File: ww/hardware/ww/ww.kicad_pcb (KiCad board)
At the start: 2 copper layers, 31 x 38 mm, 49 parts, among them J1 USB_B, J2 Conn_ARM_JTAG_SWD_10, SW1 BTN0, SW2 BTN1, U1 MCP73812T-420I-OT, U10 APA102, U11 APA102, U12 APA102, U13 APA102, U14 APA102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

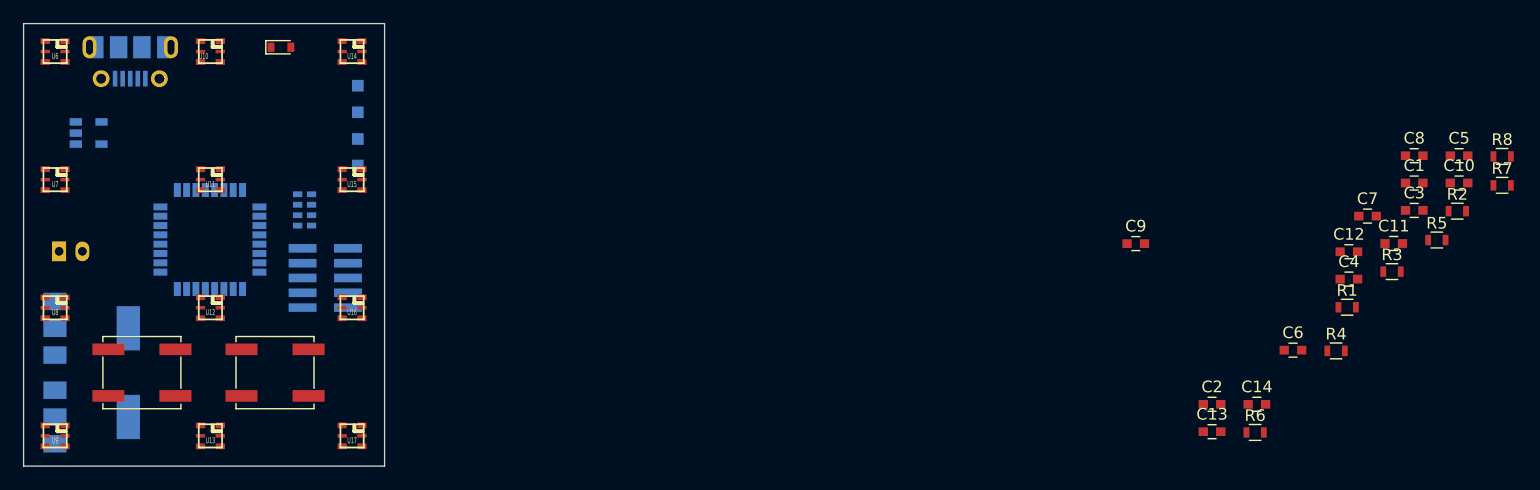
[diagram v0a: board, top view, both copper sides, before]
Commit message: Place remaining passives, no tracks yet
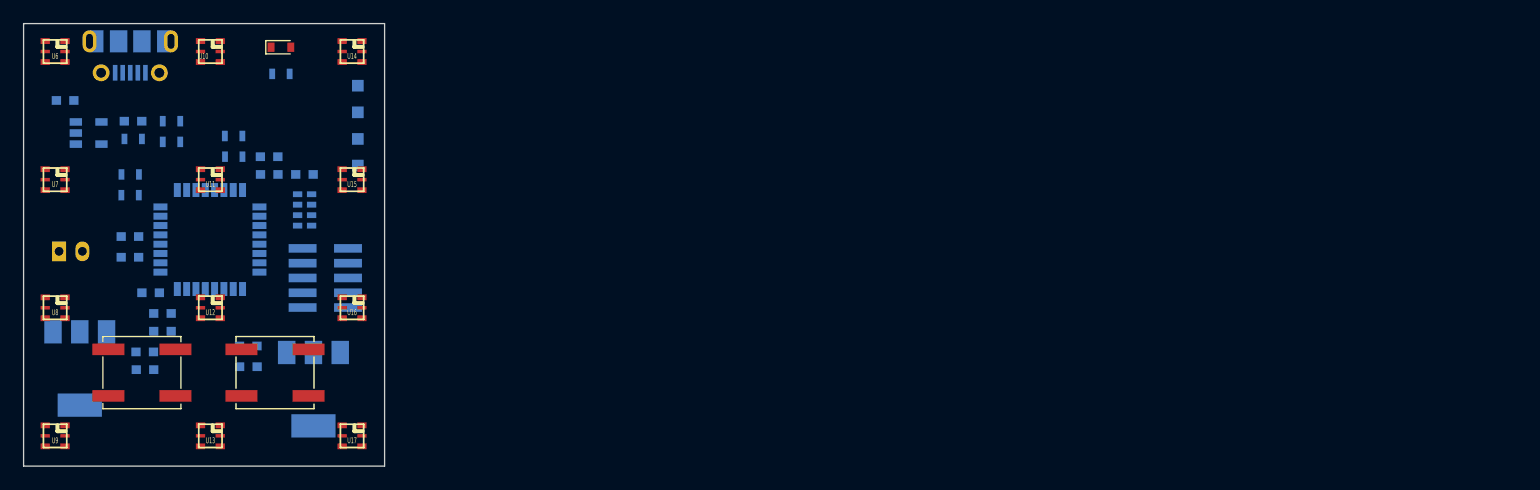
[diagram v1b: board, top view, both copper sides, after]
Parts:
- C1, C10, C11, C12, C13, C14, C2, C3, C4, C5, C6, C7, C8, C9, R1, R2, R3, R4, R5, R6, R7, R8: moved to B.Cu
- moved C3 116.2 mm to (41.7, 31.2)
- moved C5 113.0 mm to (49.0, 47.8), turned to 180 degrees
- moved R5 112.3 mm to (47.2, 39.4), turned to 180 degrees
- moved C10 112.1 mm to (50.0, 51.1), turned to 180 degrees
- moved R2 110.7 mm to (50.8, 33.0)
- moved R8 108.9 mm to (56.1, 34.3), turned to 180 degrees
- moved C7 105.6 mm to (48.5, 52.8)
- moved R3 105.4 mm to (50.8, 34.8), turned to 180 degrees
- moved R7 105.3 mm to (60.2, 29.0)
- moved R1 105.2 mm to (47.5, 34.5)
- moved R4 104.7 mm to (47.3, 37.6)
- moved C12 103.9 mm to (48.5, 54.4)
- moved C11 98.9 mm to (57.4, 54.1), turned to 180 degrees
- moved C8 98.3 mm to (59.2, 36.1)
- moved C14 97.6 mm to (47.2, 44.7), turned to 180 degrees
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
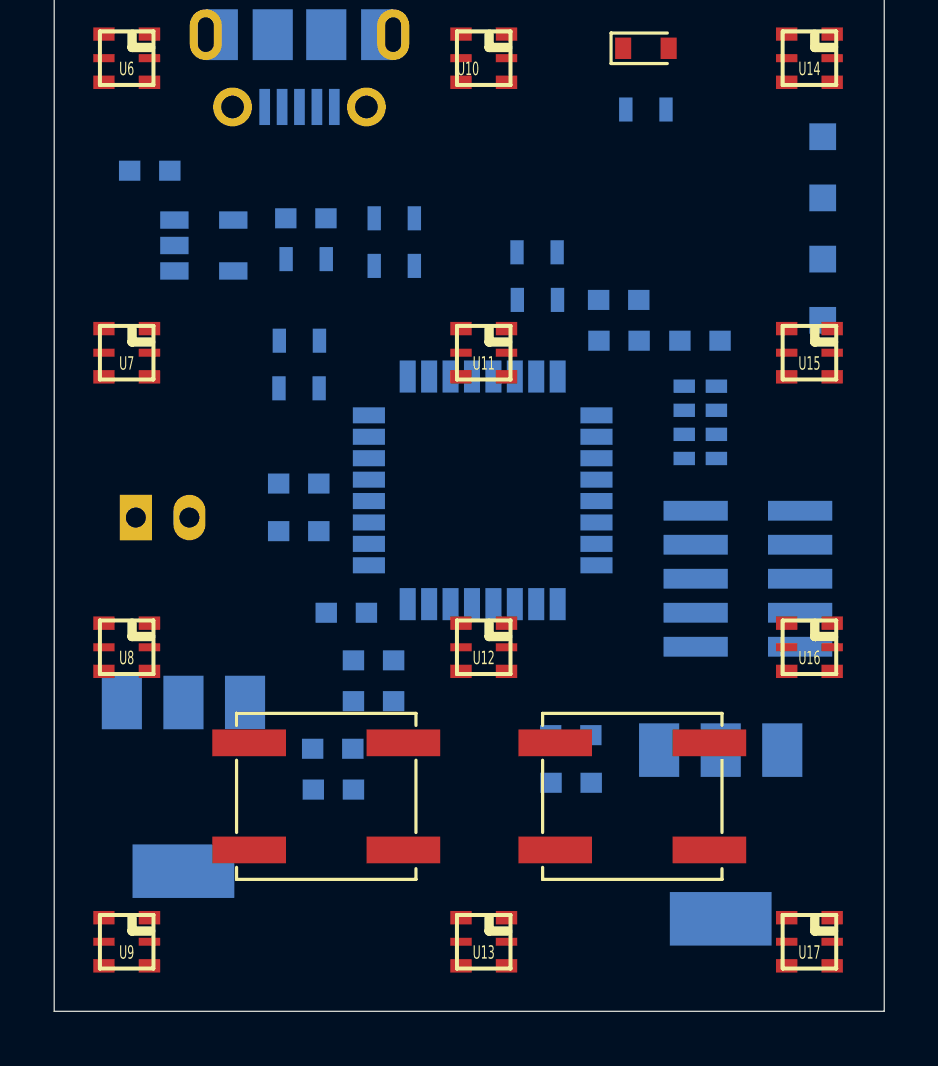
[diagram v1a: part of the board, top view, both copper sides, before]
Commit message: Use side-angled SMT JST battery connector
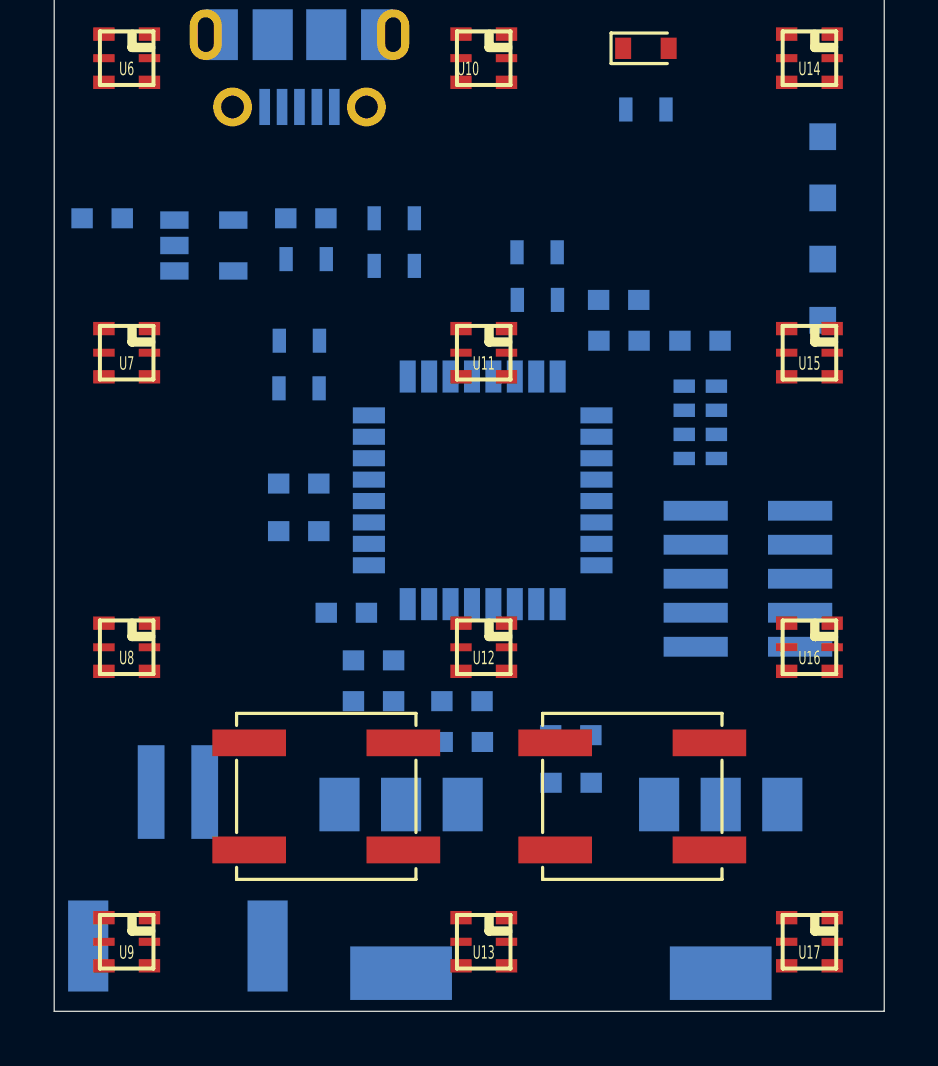
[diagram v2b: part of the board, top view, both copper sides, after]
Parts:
- BT1: footprint Connectors_JST:JST_PH_B2B-PH-K_02x2.00mm_Straight -> Connectors_JST:JST_PH_S2B-PH-SM4-TB_02x2.00mm_Angled
- moved BT1 13.2 mm to (42.7, 57.3), turned to 180 degrees
- moved U4 8.98 mm to (51.1, 58.1)
- moved C7 5.14 mm to (53.3, 51.1)
- moved C12 5.13 mm to (53.3, 52.6)
- moved C3 2.51 mm to (39.9, 33.0)
- moved U3 2.03 mm to (63.0, 58.1)
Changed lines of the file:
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@@
     (add_net "Net-(U5-Pad9)")
-  )
-  (module Connectors_JST:JST_PH_B2B-PH-K_02x2.00mm_Straight (layer B.Cu)
-    (at 41.148 44.196)
-    (descr "JST PH series connector, B2B-PH-K, top entry type, through hole, Datasheet: http://www.jst-mfg.com/product/pdf/eng/ePH.pdf")
-    (tags "connector jst ph")
-    (fp_text reference BT1 (at 1.5 2.8) (layer B.SilkS)
-      (effects (font (size 1 1) (thickness 0.15)) (justify mirror))
-    )
-    (fp_text value Battery_Cell (at 1 -3.8) (layer B.Fab)
-      (effects (font (size 1 1) (thickness 0.15)) (justify mirror))
-    )
-    (fp_text user %R (at 1 -1.5) (layer B.Fab)
-      (effects (font (size 1 1) (thickness 0.15)) (justify mirror))
-    )
-    (fp_line (start 4.45 2.2) (end -2.45 2.2) (layer B.CrtYd) (width 0.05))
-    (fp_line (start 4.45 -3.3) (end 4.45 2.2) (layer B.CrtYd) (width 0.05))
-    (fp_line (start -2.45 -3.3) (end 4.45 -3.3) (layer B.CrtYd) (width 0.05))
-    (fp_line (start -2.45 2.2) (end -2.45 -3.3) (layer B.CrtYd) (width 0.05))
-    (fp_line (start 3.95 1.7) (end -1.95 1.7) (layer B.Fab) (width 0.1))
-    (fp_line (start 3.95 -2.8) (end 3.95 1.7) (layer B.Fab) (width 0.1))
-    (fp_line (start -1.95 -2.8) (end 3.95 -2.8) (layer B.Fab) (width 0.1))
-    (fp_line (start -1.95 1.7) (end -1.95 -2.8) (layer B.Fab) (width 0.1))
-    (fp_line (start -2.35 2.1) (end -2.35 0.85) (layer B.Fab) (width 0.1))
-    (fp_line (start -1.1 2.1) (end -2.35 2.1) (layer B.Fab) (width 0.1))
-    (fp_line (start -2.35 2.1) (end -2.35 0.85) (layer B.SilkS) (width 0.12))
-    (fp_line (start -1.1 2.1) (end -2.35 2.1) (layer B.SilkS) (width 0.12))
-    (fp_line (start 1 -2.3) (end 1 -1.8) (layer B.SilkS) (width 0.12))
-    (fp_line (start 1.1 -1.8) (end 1.1 -2.3) (layer B.SilkS) (width 0.12))
-    (fp_line (start 0.9 -1.8) (end 1.1 -1.8) (layer B.SilkS) (width 0.12))
-    (fp_line (start 0.9 -2.3) (end 0.9 -1.8) (layer B.SilkS) (width 0.12))
-    (fp_line (start -0.3 1.9) (end -0.6 1.9) (layer B.SilkS) (width 0.12))
-    (fp_line (start -0.6 2) (end -0.6 1.8) (layer B.SilkS) (width 0.12))
-    (fp_line (start -0.3 2) (end -0.6 2) (layer B.SilkS) (width 0.12))
-    (fp_line (start -0.3 1.8) (end -0.3 2) (layer B.SilkS) (width 0.12))
-    (fp_line (start 4.05 -0.8) (end 3.45 -0.8) (layer B.SilkS) (width 0.12))
-    (fp_line (start 4.05 0.5) (end 3.45 0.5) (layer B.SilkS) (width 0.12))
-    (fp_line (start -2.05 -0.8) (end -1.45 -0.8) (layer B.SilkS) (width 0.12))
-    (fp_line (start -2.05 0.5) (end -1.45 0.5) (layer B.SilkS) (width 0.12))
-    (fp_line (start 1.5 1.2) (end 1.5 1.8) (layer B.SilkS) (width 0.12))
-    (fp_line (start 3.45 1.2) (end 1.5 1.2) (layer B.SilkS) (width 0.12))
-    (fp_line (start 3.45 -2.3) (end 3.45 1.2) (layer B.SilkS) (width 0.12))
-    (fp_line (start -1.45 -2.3) (end 3.45 -2.3) (layer B.SilkS) (width 0.12))
-    (fp_line (start -1.45 1.2) (end -1.45 -2.3) (layer B.SilkS) (width 0.12))
-    (fp_line (start 0.5 1.2) (end -1.45 1.2) (layer B.SilkS) (width 0.12))
-    (fp_line (start 0.5 1.8) (end 0.5 1.2) (layer B.SilkS) (width 0.12))
-    (fp_line (start 4.05 1.8) (end -2.05 1.8) (layer B.SilkS) (width 0.12))
-    (fp_line (start 4.05 -2.9) (end 4.05 1.8) (layer B.SilkS) (width 0.12))
-    (fp_line (start -2.05 -2.9) (end 4.05 -2.9) (layer B.SilkS) (width 0.12))
-    (fp_line (start -2.05 1.8) (end -2.05 -2.9) (layer B.SilkS) (width 0.12))
-    (pad 2 thru_hole oval (at 2 0) (size 1.2 1.7) (drill 0.75) (layers *.Cu *.Mask)
-      (net 1 GND))
-    (pad 1 thru_hole rect (at 0 0) (size 1.2 1.7) (drill 0.75) (layers *.Cu *.Mask)
-      (net 2 "Net-(BT1-Pad1)"))
-    (model ${KISYS3DMOD}/Connectors_JST.3dshapes/JST_PH_B2B-PH-K_02x2.00mm_Straight.wrl
-      (at (xyz 0 0 0))
-      (scale (xyz 1 1 1))
-      (rotate (xyz 0 0 0))
-    )
   )
   (module Capacitors_SMD:C_0603 (layer B.Cu)
@@
   )
   (module Capacitors_SMD:C_0603 (layer B.Cu)
-    (at 41.668 31.242)
+    (at 39.89 33.02)
     (descr "Capacitor SMD 0603, reflow soldering, AVX (see smccp.pdf)")
     (tags "capacitor 0603")
@@
   )
   (module Capacitors_SMD:C_0603 (layer B.Cu)
-    (at 48.502 52.832)
+    (at 53.328 51.054)
     (descr "Capacitor SMD 0603, reflow soldering, AVX (see smccp.pdf)")
     (tags "capacitor 0603")
@@
   )
   (module Capacitors_SMD:C_0603 (layer B.Cu)
-    (at 48.526 54.356)
+    (at 53.34 52.578)
     (descr "Capacitor SMD 0603, reflow soldering, AVX (see smccp.pdf)")
     (tags "capacitor 0603")
@@
     (tags "test point SMD pad rectangle square")
     (attr virtual)
-    (fp_text reference TP1 (at 0 1.448 90) (layer B.SilkS)
+    (fp_text reference TP1 (at 1.016 1.524 90) (layer B.SilkS)
       (effects (font (size 1 1) (thickness 0.15)) (justify mirror))
     )
@@
     (tags "test point SMD pad rectangle square")
     (attr virtual)
-    (fp_text reference TP2 (at 0 1.448 90) (layer B.SilkS)
+    (fp_text reference TP2 (at 0.508 1.524 90) (layer B.SilkS)
       (effects (font (size 1 1) (thickness 0.15)) (justify mirror))
     )
@@
     (tags "test point SMD pad rectangle square")
     (attr virtual)
-    (fp_text reference TP3 (at 0 1.448 90) (layer B.SilkS)
+    (fp_text reference TP3 (at -0.508 1.778 90) (layer B.SilkS)
       (effects (font (size 1 1) (thickness 0.15)) (justify mirror))
     )
@@
     (tags "test point SMD pad rectangle square")
     (attr virtual)
-    (fp_text reference TP4 (at 0 1.448 90) (layer B.SilkS)
+    (fp_text reference TP4 (at -1.524 1.778 90) (layer B.SilkS)
       (effects (font (size 1 1) (thickness 0.15)) (justify mirror))
     )
@@
   )
   (module TO_SOT_Packages_SMD:SOT-223 (layer B.Cu)
-    (at 62.992 56.032 270)
+    (at 62.992 58.064 270)
     (descr "module CMS SOT223 4 pins")
     (tags "CMS SOT")
@@
   )
   (module TO_SOT_Packages_SMD:SOT-223 (layer B.Cu)
-    (at 42.926 54.254 270)
+    (at 51.054 58.064 270)
     (descr "module CMS SOT223 4 pins")
     (tags "CMS SOT")
     (attr smd)
-    (fp_text reference U4 (at 0 4.064 90) (layer B.SilkS)
+    (fp_text reference U4 (at 0.356 -4.826 90) (layer B.SilkS)
       (effects (font (size 1 1) (thickness 0.15)) (justify mirror))
     )
@@
       (net 61 "Net-(U13-Pad5)"))
   )
+  (module Connectors_JST:JST_PH_S2B-PH-SM4-TB_02x2.00mm_Angled (layer B.Cu)
+    (at 42.72 57.323 180)
+    (descr "JST PH series connector, S2B-PH-SM4-TB, side entry type, surface mount, Datasheet: http://www.jst-mfg.com/product/pdf/eng/ePH.pdf")
+    (tags "connector jst ph")
+    (attr smd)
+    (fp_text reference BT1 (at 0 5.625 180) (layer B.SilkS)
+      (effects (font (size 1 1) (thickness 0.15)) (justify mirror))
+    )
+    (fp_text value Battery_Cell (at 0 -5.375 180) (layer B.Fab)
+      (effects (font (size 1 1) (thickness 0.15)) (justify mirror))
+    )
+    (fp_text user %R (at 0 -1.5 180) (layer B.Fab)
+      (effects (font (size 1 1) (thickness 0.15)) (justify mirror))
+    )
+    (fp_line (start 4.6 5.13) (end -4.6 5.13) (layer B.CrtYd) (width 0.05))
+    (fp_line (start 4.6 -5.07) (end 4.6 5.13) (layer B.CrtYd) (width 0.05))
+    (fp_line (start -4.6 -5.07) (end 4.6 -5.07) (layer B.CrtYd) (width 0.05))
+    (fp_line (start -4.6 5.13) (end -4.6 -5.07) (layer B.CrtYd) (width 0.05))
+    (fp_line (start -1 0.625) (end 0 1.625) (layer B.Fab) (width 0.1))
+    (fp_line (start -2 1.625) (end -1 0.625) (layer B.Fab) (width 0.1))
+    (fp_line (start -1.775 1.725) (end -1.775 4.625) (layer B.SilkS) (width 0.12))
+    (fp_line (start -2.325 -4.475) (end 2.325 -4.475) (layer B.SilkS) (width 0.12))
+    (fp_line (start 3.05 1.725) (end 1.775 1.725) (layer B.SilkS) (width 0.12))
+    (fp_line (start 3.05 3.325) (end 3.05 1.725) (layer B.SilkS) (width 0.12))
+    (fp_line (start 4.05 3.325) (end 3.05 3.325) (layer B.SilkS) (width 0.12))
+    (fp_line (start 4.05 -0.9) (end 4.05 3.325) (layer B.SilkS) (width 0.12))
+    (fp_line (start -4.05 3.325) (end -4.05 -0.9) (layer B.SilkS) (width 0.12))
+    (fp_line (start -3.05 3.325) (end -4.05 3.325) (layer B.SilkS) (width 0.12))
+    (fp_line (start -3.05 1.725) (end -3.05 3.325) (layer B.SilkS) (width 0.12))
+    (fp_line (start -1.775 1.725) (end -3.05 1.725) (layer B.SilkS) (width 0.12))
+    (fp_line (start 3.15 1.625) (end -3.15 1.625) (layer B.Fab) (width 0.1))
+    (fp_line (start 3.15 3.225) (end 3.15 1.625) (layer B.Fab) (width 0.1))
+    (fp_line (start 3.95 3.225) (end 3.15 3.225) (layer B.Fab) (width 0.1))
+    (fp_line (start 3.95 -4.375) (end 3.95 3.225) (layer B.Fab) (width 0.1))
+    (fp_line (start -3.95 -4.375) (end 3.95 -4.375) (layer B.Fab) (width 0.1))
+    (fp_line (start -3.95 3.225) (end -3.95 -4.375) (layer B.Fab) (width 0.1))
+    (fp_line (start -3.15 3.225) (end -3.95 3.225) (layer B.Fab) (width 0.1))
+    (fp_line (start -3.15 1.625) (end -3.15 3.225) (layer B.Fab) (width 0.1))
+    (pad "" smd rect (at 3.35 -2.875 180) (size 1.5 3.4) (layers B.Cu B.Paste B.Mask))
+    (pad "" smd rect (at -3.35 -2.875 180) (size 1.5 3.4) (layers B.Cu B.Paste B.Mask))
+    (pad 2 smd rect (at 1 2.875 180) (size 1 3.5) (layers B.Cu B.Paste B.Mask)
+      (net 1 GND))
+    (pad 1 smd rect (at -1 2.875 180) (size 1 3.5) (layers B.Cu B.Paste B.Mask)
+      (net 2 "Net-(BT1-Pad1)"))
+    (model ${KISYS3DMOD}/Connectors_JST.3dshapes/JST_PH_S2B-PH-SM4-TB_02x2.00mm_Angled.wrl
+      (at (xyz 0 0 0))
+      (scale (xyz 1 1 1))
+      (rotate (xyz 0 0 0))
+    )
+  )
   (gr_line (start 69.1 24.638) (end 69.1 62.638) (layer Edge.Cuts) (width 0.05))

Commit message: Add initial AS102 tracks
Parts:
- moved U3 1.28 mm to (64.3, 57.9)
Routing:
- net /LED_CLK3: track 0.00 -> 34.9 mm
- net /LED_SDI3: track 0.00 -> 34.8 mm
- net /LED_SDI1: track 0.00 -> 32.8 mm
- net /LED_SDI2: track 0.00 -> 32.5 mm
- net /LED_CLK2: track 0.00 -> 31.3 mm
- net /LED_CLK1: track 0.00 -> 31.0 mm
- net Net-(U10-Pad2): track 0.00 -> 16.8 mm
- net Net-(U10-Pad1): track 0.00 -> 15.0 mm
- net Net-(U11-Pad1): track 0.00 -> 14.4 mm
- net Net-(U12-Pad1): track 0.00 -> 14.2 mm
- net Net-(U13-Pad1): track 0.00 -> 14.2 mm
- net Net-(U10-Pad6): track 0.00 -> 13.3 mm
- net Net-(U11-Pad6): track 0.00 -> 13.2 mm
- net Net-(U13-Pad6): track 0.00 -> 13.0 mm
- net Net-(U12-Pad6): track 0.00 -> 13.0 mm
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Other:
- rule trace_min: 0.2 -> 0.127
- rule via_min_size: 0.4 -> 0.6
